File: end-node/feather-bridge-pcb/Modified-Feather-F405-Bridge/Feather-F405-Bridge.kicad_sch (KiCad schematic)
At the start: 15 parts, among them J1 Conn_01x06, J2 Conn_01x06, J3 Conn_02x06_Odd_Even, SW1 SW_SPST, SW2 SW_SPST, U1 LoRa Radio FeatherWing, U2 NUD3112LT1, U3 NUD3112LT1

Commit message: cleanup schematic
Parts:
- U2, U3: footprint SOT-23_ONS -> Footprints:SOT-23; symbol 2023-04-07_15-25-17:NUD3112LT1 -> Symbols:Q_NMOS_GSD
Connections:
- net REMOTE_DFU: now reaches J1.2 (Pin_2), R3.1, U3.1 (G)
- net REMOTE_RST: now reaches J1.6 (Pin_6), R2.2, U2.1 (G)
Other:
- moved on the sheet: C1, JP1, R1, R2, R3, SW1, SW2

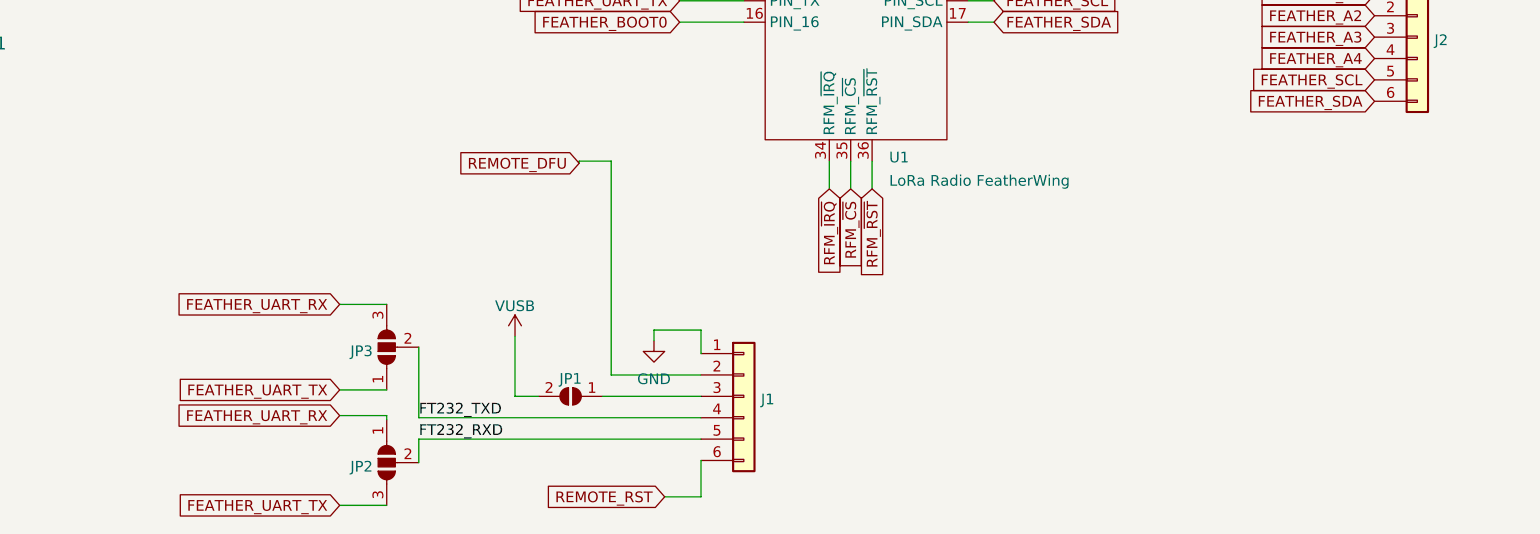
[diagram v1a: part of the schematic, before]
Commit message: Remove UART RX/TX crossover SB, fix resistor footprints, add separate header for remote dfu/rst, fancy logo
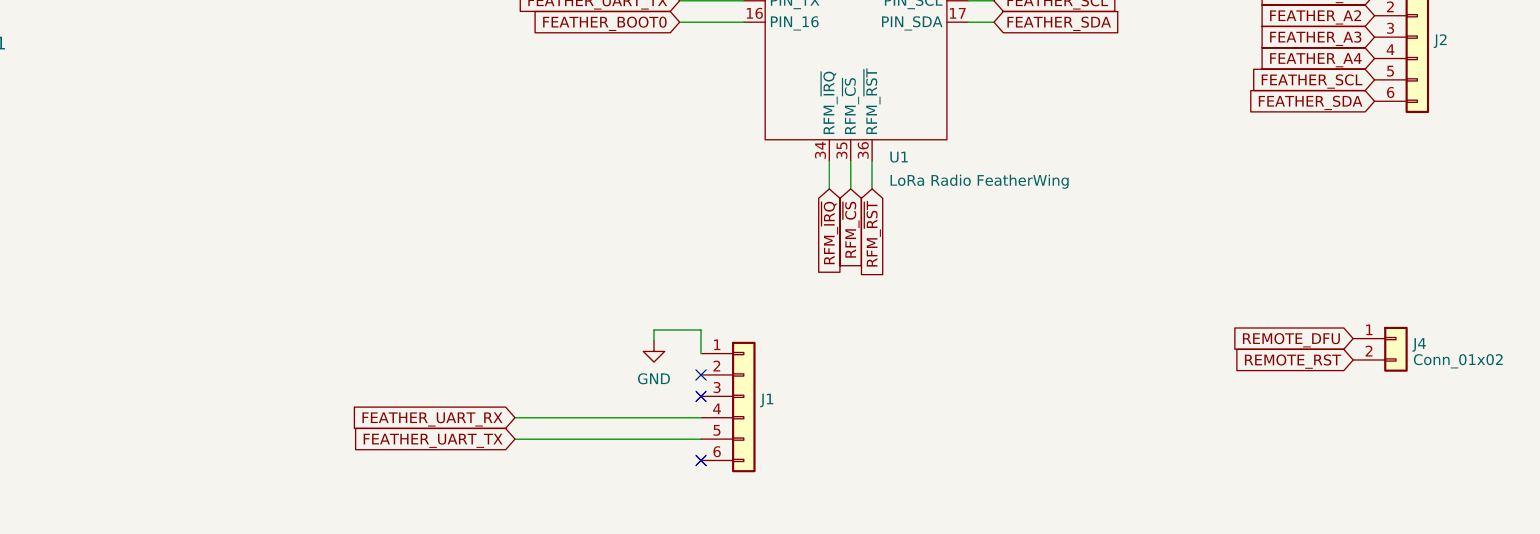
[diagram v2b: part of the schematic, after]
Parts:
- removed JP1: SolderJumper_2_Open, Footprints:SolderJumper-2_P1.3mm_Open_TrianglePad1.0x1.5mm, symbol Symbols:SolderJumper_2_Open
- removed JP2, JP3: SolderJumper_3_Open, Footprints:SolderJumper-3_P2.0mm_Open_TrianglePad1.0x1.5mm, symbol Symbols:SolderJumper_3_Open
- added J4: Conn_01x02, Footprints:PinHeader_1x02_P2.54mm_Horizontal, symbol Symbols:Conn_01x02
- C1: footprint Footprints:C_Rect_L4.0mm_W2.5mm_P2.50mm -> Footprints:C_Disc_D3.0mm_W1.6mm_P2.50mm
- R1, R2, R3: footprint Footprints:R_Box_L8.4mm_W2.5mm_P5.08mm -> Footprints:R_Axial_DIN0207_L6.3mm_D2.5mm_P10.16mm_Horizontal
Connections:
- net FT232_RXD is gone; now on net FEATHER_UART_TX: J1.5 (Pin_5)
- net FT232_TXD is gone; now on net FEATHER_UART_RX: J1.4 (Pin_4)
- net REMOTE_DFU: now also J4.1 (Pin_1); no longer J1.2 (Pin_2)
- net REMOTE_RST: now also J4.2 (Pin_2); no longer J1.6 (Pin_6)
- no-connect marks 2 -> 5

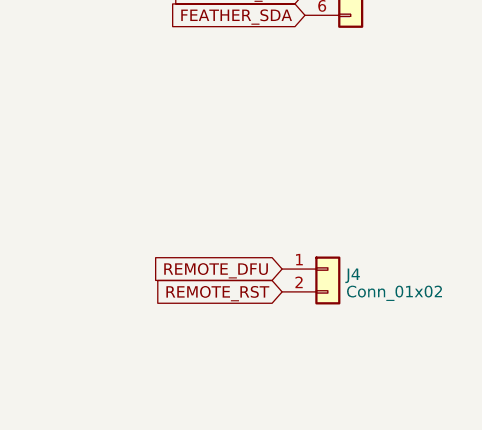
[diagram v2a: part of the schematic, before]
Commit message: tweak some lines for future changes with BLE
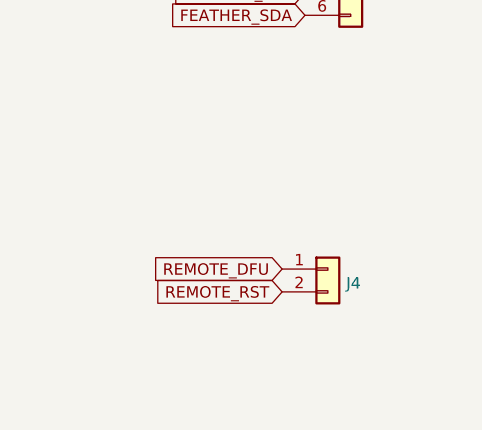
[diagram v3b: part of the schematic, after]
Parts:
- J4: value Conn_01x02 -> ~
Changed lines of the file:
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@@
   (symbol (lib_id "Symbols:Conn_01x02") (at 232.41 132.842 0) (unit 1)
     (in_bom yes) (on_board yes) (dnp no) (fields_autoplaced)
-    (property "Reference" "J4" (at 234.442 133.4683 0)
+    (property "Reference" "J4" (at 234.442 134.4288 0)
       (effects (font (size 1.27 1.27)) (justify left))
     )
-    (property "Value" "Conn_01x02" (at 234.442 135.3893 0)
+    (property "Value" "~" (at 234.442 135.3893 0)
       (effects (font (size 1.27 1.27)) (justify left))
     )
